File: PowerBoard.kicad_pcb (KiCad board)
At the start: 4 copper layers, 50 x 60 mm, 65 parts, among them Q1 SQJ409EP

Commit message: finished first converter
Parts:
- R11, R17, R18, R9: moved to B.Cu
- moved C15 106.9 mm to (80.7, 115.9)
- moved C22 99.9 mm to (94.6, 123.6)
- moved U5 98.2 mm to (112.3, 149.2)
- moved C24 98.2 mm to (95.7, 144.1)
- moved C5 98.2 mm to (95.8, 133.9)
- moved U9 98.2 mm to (113.6, 159.3)
- moved R9 57.2 mm to (135.5, 116.8), turned to 180 degrees
- moved R11 56.4 mm to (137.1, 114.1), turned to 90 degrees
- moved R18 51.7 mm to (135.5, 114.1), turned to -90 degrees
- moved R17 50.2 mm to (133.7, 112.4), turned to -90 degrees
- moved L2 0.79 mm to (140.9, 101.1)
- moved C17 0.66 mm to (135.6, 109.7)
- moved C29 0.63 mm to (146.1, 109.6)
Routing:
- net +6V: track 0.00 -> 44.4 mm, vias 0 -> 4
- net /PGOOD_6V: track 0.00 -> 6.38 mm, vias 0 -> 2
- net Net-(U4-EN/SYNC): track 0.00 -> 6.15 mm
- net Net-(U4-VCC): track 0.00 -> 5.46 mm, vias 0 -> 2
- net Net-(U4-RT): track 0.00 -> 2.04 mm

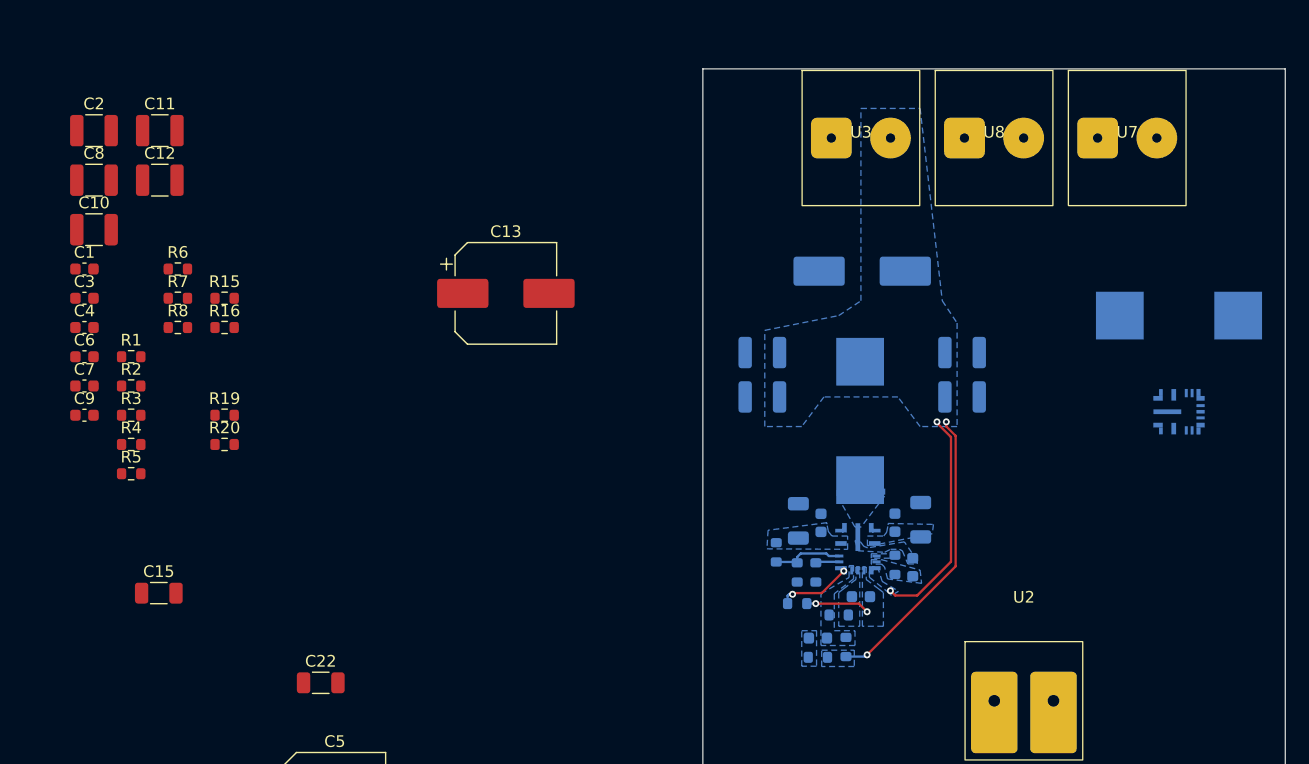
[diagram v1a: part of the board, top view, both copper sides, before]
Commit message: added second buck
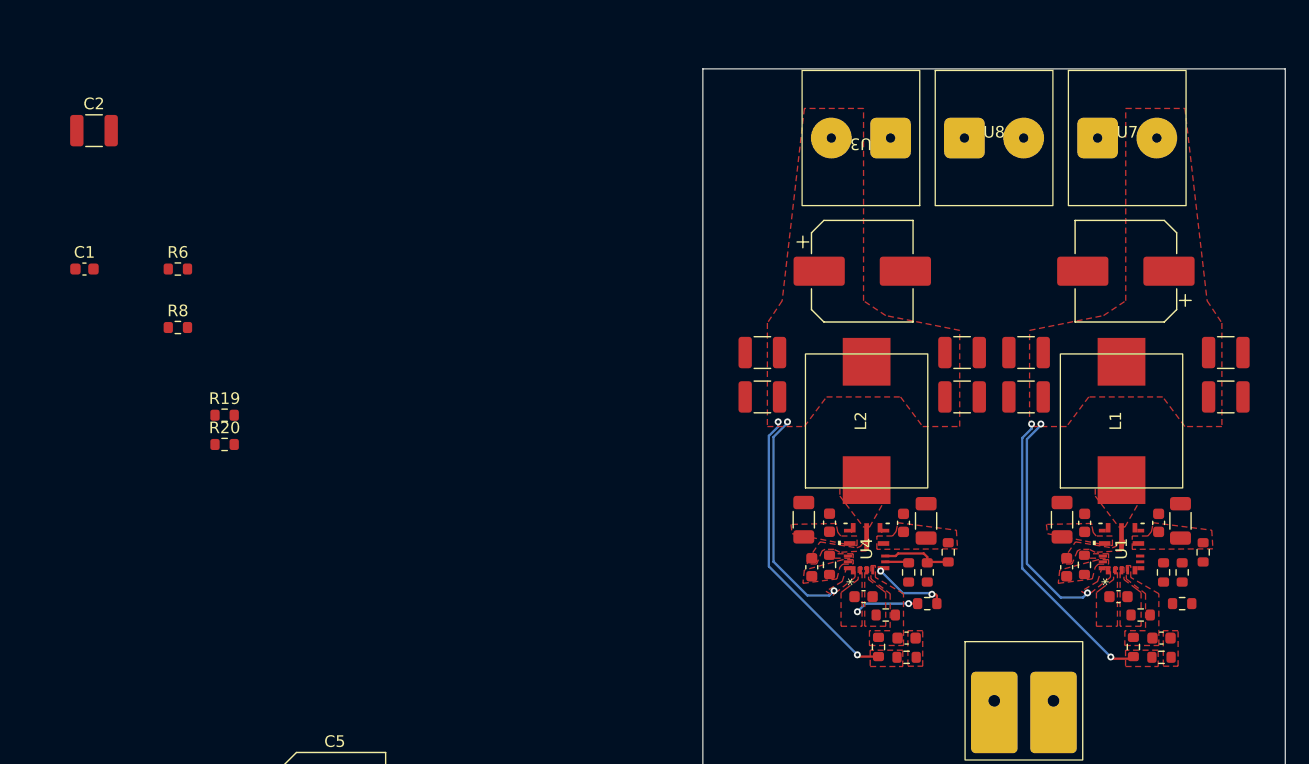
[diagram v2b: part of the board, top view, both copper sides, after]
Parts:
- C16, C17, C18, C19, C20, C21, C23, C25, C26, C27, C28, C29, L1, L2, R10, R11, R12, R13, R14, R17, R18, R9, U1, U4: moved to F.Cu
- moved C8 98.3 mm to (172.3, 95.2)
- moved C10 98.2 mm to (172.3, 99.1)
- moved C9 94.4 mm to (166.8, 119.8), turned to 180 degrees
- moved C4 93.7 mm to (166.5, 109.9), turned to 90 degrees
- moved R1 92.7 mm to (168.5, 116.8)
- moved C6 91.1 mm to (163.1, 116.2)
- moved R3 90.9 mm to (166.8, 121.4)
- moved R2 90.1 mm to (166.9, 114.1), turned to -90 degrees
- moved C3 88.0 mm to (160.2, 109.9), turned to 90 degrees
- moved R4 87.8 mm to (164.4, 120.5), turned to 90 degrees
- moved R5 87.5 mm to (165.0, 117.8), turned to 180 degrees
- moved R16 86.2 mm to (170.3, 112.4), turned to -90 degrees
- moved C7 85.7 mm to (158.6, 113.7), turned to -90 degrees
- moved R15 85.5 mm to (168.5, 114.1), turned to -90 degrees
- moved R7 81.1 mm to (160.2, 113.5), turned to -90 degrees
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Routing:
- net +5V: track 0.00 -> 25.1 mm, vias 0 -> 2
- net +6V: track 44.4 -> 63.4 mm, vias 4 -> 6
- added copper zone on F.Cu, net +5V
- added copper zone on F.Cu, net +6V
- added copper zone on F.Cu, net +VBAT_PRO
- added copper zone on F.Cu, net GND
- added copper zone on F.Cu, net Net-(C28-Pad1)
- added copper zone on F.Cu, net Net-(C9-Pad1)
- added copper zone on F.Cu, net Net-(U1-FB)
- added copper zone on F.Cu, net Net-(U1-VCC)
- added copper zone on F.Cu, net Net-(U4-CBOOT)
- added copper zone on F.Cu, net Net-(U4-FB)
- added copper zone on F.Cu, net Net-(U4-RBOOT)
- added copper zone on F.Cu, net Net-(U4-SW)
- added copper zone on F.Cu, net Net-(U4-VCC)
- removed copper zone on B.Cu, net +6V
- removed copper zone on B.Cu, net +VBAT_PRO
- removed copper zone on B.Cu, net GND
- removed copper zone on B.Cu, net Net-(C28-Pad1)
- removed copper zone on B.Cu, net Net-(U4-CBOOT)
- removed copper zone on B.Cu, net Net-(U4-FB)
- removed copper zone on B.Cu, net Net-(U4-RBOOT)
- removed copper zone on B.Cu, net Net-(U4-SW)
- removed copper zone on B.Cu, net Net-(U4-VCC)

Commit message: finsihed main routing
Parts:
- added G***: LOGO, powerBoardSchool:testNeutron, F.Cu at (131.4, 85.1)
- added G***: LOGO, powerBoardSchool:arrowNeutronPB, F.Cu at (131.2, 114.9)
- added U10: ~, powerBoardSchool:Unbenannt, F.Cu at (131.4, 126.9)
- added U11: ~, powerBoardSchool:Unbenannt, F.Cu at (131.4, 75.0)
- added U12: ~, powerBoardSchool:Unbenannt, F.Cu at (173.4, 74.9)
- added U13: ~, powerBoardSchool:Unbenannt, F.Cu at (173.4, 126.9)
- D1: footprint Diode_SMD:D_SMA -> Package_TO_SOT_SMD:SOT-23-3
- moved D1 142.3 mm to (172.7, 90.3), turned to -90 degrees
- moved U6 139.4 mm to (173.4, 81.1), turned to 90 degrees
- moved D5 131.9 mm to (155.4, 86.6), turned to -90 degrees
- moved D4 128.2 mm to (152.4, 86.6), turned to -90 degrees
- moved D3 124.4 mm to (149.4, 86.6), turned to -90 degrees
- moved D2 119.7 mm to (150.4, 105.1), turned to 90 degrees
- moved Q1 112.2 mm to (153.5, 115.8), turned to -90 degrees
- moved C2 98.2 mm to (172.8, 86.2)
- moved C1 96.6 mm to (170.7, 81.0), turned to -90 degrees
- moved U9 77.5 mm to (175.8, 113.0), turned to -90 degrees
- moved U5 76.0 mm to (174.5, 105.4)
- moved R6 74.0 mm to (154.1, 106.2)
- moved C24 70.9 mm to (164.2, 126.0), turned to 180 degrees
- moved R20 70.3 mm to (155.4, 90.2), turned to 90 degrees
- moved R8 67.1 mm to (149.4, 90.2), turned to 90 degrees
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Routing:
- net /PGOOD_6V: track 6.38 -> 47.5 mm, vias 2 -> 3
- net +5V: track 25.1 -> 54.6 mm, vias 2 -> 39
- net +6V: track 63.4 -> 36.3 mm, vias 6 -> 33
- net +3V3: track 0.00 -> 20.9 mm, vias 0 -> 9
- net Net-(U4-FB): track 0.00 -> 10.1 mm
- net /PGOOD_5V: track 0.00 -> 9.53 mm
- net Net-(D2-A): track 0.00 -> 9.21 mm
- net Net-(U1-FB): track 0.00 -> 9.12 mm
- net Net-(U1-EN/SYNC): track 0.00 -> 6.21 mm
- net Net-(U1-VCC): track 0.00 -> 6.11 mm, vias 0 -> 2
- net GND: track 0.00 -> 2.28 mm, vias 0 -> 199
- net Net-(U1-RT): track 0.00 -> 2.04 mm
- net Net-(C28-Pad1): track 0.00 -> 2.04 mm
- net Net-(D5-A): track 0.00 -> 1.98 mm
- net Net-(D4-A): track 0.00 -> 1.98 mm
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- added copper zone on B.Cu, net +3V3
- added copper zone on F.Cu, net +3V3
- added copper zone on In2.Cu, net +5V
- added copper zone on In2.Cu, net +6V
- added copper zone on In2.Cu, net +VBAT_PRO
- added copper zone on In1.Cu, net GND
- added copper zone on F.Cu, net Net-(Q1-D)
- added copper zone on In2.Cu, net Net-(Q1-D)
- added copper zone on F.Cu, net Net-(U1-CBOOT)
- added copper zone on F.Cu, net Net-(U1-RBOOT)
- added copper zone on F.Cu, net Net-(U1-SW)
- removed copper zone on F.Cu, net Net-(C28-Pad1)
- removed copper zone on F.Cu, net Net-(U1-FB)
- removed copper zone on F.Cu, net Net-(U4-FB)
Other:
- outline, holes or cut-outs redrawn
- board text added: "+3V3"
- board text added: "+5V"
- board text added: "+6V"
- board text added: "6V GND"
- board text added: "GND"
- board text added: "GND +3V3"
- board text added: "GND 5V"
- board text added: "GND GND PG5 PG6"
- board text added: "GND VPRT"
- board text added: "VIN"
- board text added: "VOUT"

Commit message: final
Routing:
- net /PGOOD_5V: track 9.53 -> 16.1 mm
- net GND: vias 199 -> 198
- net +VBAT_PRO: vias 57 -> 71
- net +6V: vias 33 -> 32
- net +5V: vias 39 -> 38

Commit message: increased hole size
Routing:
- added copper zone on B.Cu, net +5V
- added copper zone on B.Cu, net +6V
- added copper zone on B.Cu, net +VBAT_PRO
- added copper zone on B.Cu, net GND
- added copper zone on B.Cu, net Net-(Q1-D)
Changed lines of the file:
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@@
 			(drillshape 0)
 			(scaleselection 1)
-			(outputdirectory "C:/Users/finnu/Downloads/")
+			(outputdirectory "C:/Users/schule/Downloads/")
 		)
 	)
@@
 	)
 	(zone
+		(net "GND")
+		(layer "B.Cu")
+		(hatch none 0.5)
+		(priority 52)
+		(connect_pads yes
+			(clearance 0.2)
+		)
+		(min_thickness 0.025)
+		(fill yes
+			(thermal_gap 0.5)
+			(thermal_bridge_width 0.5)
+			(island_removal_mode 1)
+		)
+		(polygon
+			(pts
+				(xy 141.605 71.882) (xy 152.273 71.882) (xy 152.4 82.6516) (xy 141.6558 82.635)
+			)
+		)
+	)
+	(zone
+		(net "GND")
+		(layer "B.Cu")
+		(hatch none 0.5)
+		(priority 54)
+		(connect_pads yes
+			(clearance 0.2)
+		)
+		(min_thickness 0.025)
+		(fill yes
+			(thermal_gap 0.5)
+			(thermal_bridge_width 0.5)
+			(island_removal_mode 1)
+		)
+		(polygon
+			(pts
+				(xy 157.353 72.136) (xy 163.195 72.136) (xy 163.195 81.026) (xy 157.353 81.026)
+			)
+		)
+	)
+	(zone
+		(net "GND")
+		(layer "B.Cu")
+		(hatch none 0.5)
+		(priority 56)
+		(connect_pads yes
+			(clearance 0.2)
+		)
+		(min_thickness 0.025)
+		(fill yes
+			(thermal_gap 0.5)
+			(thermal_bridge_width 0.5)
+			(island_removal_mode 1)
+		)
+		(polygon
+			(pts
+				(xy 141.104219 121.624) (xy 152.1206 121.6152) (xy 152.4 131.826) (xy 140.97 131.826)
+			)
+		)
+	)
+	(zone
+		(net "+VBAT_PRO")
+		(layer "B.Cu")
+		(hatch none 0.5)
+		(priority 53)
+		(connect_pads yes
+			(clearance 0.2)
+		)
+		(min_thickness 0.025)
+		(fill yes
+			(thermal_gap 0.5)
+			(thermal_bridge_width 0.5)
+			(island_removal_mode 1)
+		)
+		(polygon
+			(pts
+				(xy 156.9 71.9) (xy 156.9 82.5) (xy 152.654 82.5) (xy 152.8 71.9)
+			)
+		)
+	)
+	(zone
+		(net "Net-(Q1-D)")
+		(layer "B.Cu")
+		(hatch none 0.5)
+		(priority 57)
+		(connect_pads yes
+			(clearance 0.2)
+		)
+		(min_thickness 0.025)
+		(fill yes
+			(thermal_gap 0.5)
+			(thermal_bridge_width 0.5)
+			(island_removal_mode 1)
+		)
+		(polygon
+			(pts
+				(xy 157.48 131.953) (xy 157.45 120.065) (xy 152.654 120.065) (xy 152.654 131.953)
+			)
+		)
+	)
+	(zone
+		(net "+6V")
+		(layer "B.Cu")
+		(hatch none 0.5)
+		(priority 51)
+		(connect_pads yes
+			(clearance 0.2)
+		)
+		(min_thickness 0.025)
+		(fill yes
+			(thermal_gap 0.5)
+			(thermal_bridge_width 0.5)
+			(island_removal_mode 1)
+		)
+		(polygon
+			(pts
+				(xy 136.290846 72.771) (xy 141.195 72.771) (xy 141.1732 82.6516) (xy 136.1186 82.635)
+			)
+		)
+	)
+	(zone
 		(net "+3V3")
 		(layer "B.Cu")
@@
 			)
 		)
+	)
+	(zone
+		(net "+5V")
+		(layer "B.Cu")
+		(hatch none 0.5)
+		(priority 55)
+		(connect_pads yes
+			(clearance 0.2)
+		)
+		(min_thickness 0.025)
+		(fill yes
+			(thermal_gap 0.5)
+			(thermal_bridge_width 0.5)
+			(island_removal_mode 1)
+		)
+		(polygon
+			(pts
+				(xy 163.703 72.517) (xy 168.804167 72.517) (xy 168.88 82.635) (xy 163.83 82.635)
+			)
+		)

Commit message: added LCSC codes
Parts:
- R2: value 33k -> 33.2k
- U3, U7, U8: footprint PowerBoard:ScrewTerminal -> PowerBoard:HighCurrentPad
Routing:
- net +5V: track 54.6 -> 44.9 mm
